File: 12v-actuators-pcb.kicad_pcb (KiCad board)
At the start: 2 copper layers, 0 parts

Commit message: First placement draft
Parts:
- added C1: 10uF, Capacitor_SMD:C_0805_2012Metric, F.Cu at (27.5, 27.8)
- added C10: 100nF, Capacitor_SMD:C_0603_1608Metric, F.Cu at (61.2, 10.8)
- added C11: 100nF, Capacitor_SMD:C_0603_1608Metric, F.Cu at (61.2, 13.3)
- added C12: 10uF, Capacitor_SMD:C_0805_2012Metric, F.Cu at (81.7, 11.2)
- added C13: 470pF, Capacitor_SMD:C_0603_1608Metric, F.Cu at (61.2, 15.8)
- added C14: 470pF, Capacitor_SMD:C_0603_1608Metric, F.Cu at (65.2, 0.76)
- added C15: 100nF, Capacitor_SMD:C_0603_1608Metric, F.Cu at (65.2, 3.27)
- added C16: 470pF, Capacitor_SMD:C_0603_1608Metric, F.Cu at (65.2, 5.78)
- added C17: 100nF, Capacitor_SMD:C_0603_1608Metric, F.Cu at (35.9, 53.3)
- added C18: 470uF, Capacitor_THT:C_Radial_D8.0mm_H11.5mm_P3.50mm, F.Cu at (187.5, 117.2)
- added C19: 470uF, Capacitor_THT:C_Radial_D8.0mm_H11.5mm_P3.50mm, F.Cu at (187.0, 107.8)
- added C2: 1nF, Capacitor_SMD:C_0603_1608Metric, F.Cu at (22.6, 43.7)
- added C20: 100nF, Capacitor_SMD:C_0603_1608Metric, F.Cu at (35.9, 55.8)
- added C21: 220nF, Capacitor_SMD:C_0603_1608Metric, F.Cu at (63.6, 62.9)
- added C22: 15nF, Capacitor_SMD:C_0603_1608Metric, F.Cu at (63.6, 65.5)
- added C23: 15nF, Capacitor_SMD:C_0603_1608Metric, F.Cu at (63.6, 68.0)
- added C24: 100nF, Capacitor_SMD:C_0603_1608Metric, F.Cu at (63.6, 70.5)
- added C25: 1uF, Capacitor_SMD:C_0805_2012Metric, F.Cu at (71.9, 70.4)
- added C3: 10uF, Capacitor_SMD:C_0805_2012Metric, F.Cu at (27.5, 30.8)
- added C4: 10uF, Capacitor_SMD:C_0805_2012Metric, F.Cu at (27.5, 33.8)
- added C5: 100nF, Capacitor_SMD:C_0603_1608Metric, F.Cu at (61.2, 0.76)
- added C6: 100nF, Capacitor_SMD:C_0603_1608Metric, F.Cu at (61.2, 3.27)
- added C7: 10uF, Capacitor_SMD:C_0805_2012Metric, F.Cu at (81.7, 8.21)
- added C8: 470pF, Capacitor_SMD:C_0603_1608Metric, F.Cu at (61.2, 5.78)
- added C9: 470pF, Capacitor_SMD:C_0603_1608Metric, F.Cu at (61.2, 8.29)
- added D1: ~, Diode_SMD:D_SOD-323, F.Cu at (77.4, 0.97)
- added D2: ~, Diode_SMD:D_SOD-323, F.Cu at (77.4, 3.92)
- added D3: ~, Diode_SMD:D_SOD-323, F.Cu at (77.4, 6.88)
- added D4: ~, Diode_SMD:D_SOD-323, F.Cu at (77.4, 9.82)
- added D5: ~, Diode_SMD:D_SOD-323, F.Cu at (77.4, 12.8)
- added D6: ~, ComponentsEvo:DO-214AB, F.Cu at (176.5, 106.5)
- added D7: 14.6V, Diode_SMD:D_SOD-323, F.Cu at (54.5, 72.2)
- added D8: LED, LED_SMD:LED_0603_1608Metric, F.Cu at (54.4, 75.0)
- added J1: 12V_C_MOT, ConnectorsEvo:691321100002, F.Cu at (196.0, 105.6)
- added J10: ESC_35_2_P, ConnectorsEvo:691321100002, F.Cu at (178.6, 66.3)
- added J11: MOTOR_15_2, Connector_PinHeader_2.54mm:PinHeader_1x03_P2.54mm_Vertical, F.Cu at (164.4, 74.0)
- added J12: ESC_35_2_S, Connector_PinHeader_2.54mm:PinHeader_1x03_P2.54mm_Vertical, F.Cu at (147.3, 63.8)
- added J13: MOTOR_15_3, Connector_PinHeader_2.54mm:PinHeader_1x03_P2.54mm_Vertical, F.Cu at (174.0, 74.0)
- added J14: 690367280876, ConnectorsEvo:690367280876, F.Cu at (156.8, 65.4)
- added J2: 3.5mm WR-TBL, ConnectorsEvo:691321100002, F.Cu at (196.0, 115.7)
- added J3: 690367280676, ConnectorsEvo:690367280676, F.Cu at (135.7, 65.5)
- added J4: LCD_DEG, Connector_PinHeader_2.54mm:PinHeader_1x03_P2.54mm_Vertical, F.Cu at (148.1, 74.0)
- added J5: CAN, Connector_PinHeader_2.54mm:PinHeader_1x02_P2.54mm_Vertical, F.Cu at (125.5, 69.2)
- added J6: ESC_35_1_P, ConnectorsEvo:691321100002, F.Cu at (168.8, 66.3)
- added J7: LED_EN, Connector_PinHeader_2.54mm:PinHeader_1x02_P2.54mm_Vertical, F.Cu at (134.0, 74.0)
- added J8: MOTOR_15_1, Connector_PinHeader_2.54mm:PinHeader_1x03_P2.54mm_Vertical, F.Cu at (154.3, 74.0)
- added J9: ESC_35_1_S, Connector_PinHeader_2.54mm:PinHeader_1x03_P2.54mm_Vertical, F.Cu at (143.5, 63.8)
- added Q1: G2302, Package_TO_SOT_SMD:SOT-23, F.Cu at (71.7, 29.0)
- added Q2: G2302, Package_TO_SOT_SMD:SOT-23, F.Cu at (71.7, 33.4)
- added Q3: G2302, Package_TO_SOT_SMD:SOT-23, F.Cu at (71.7, 37.9)
- added Q4: G2302, Package_TO_SOT_SMD:SOT-23, F.Cu at (71.7, 42.3)
- added Q5: G2302, Package_TO_SOT_SMD:SOT-23, F.Cu at (71.7, 46.8)
- added Q6: SUM110P06-08L, Package_TO_SOT_SMD:TO-252-2, F.Cu at (177.5, 115.2)
- added Q7: 2N7002, Package_TO_SOT_SMD:SOT-23, F.Cu at (49.9, 70.0)
- added Q8: 2N7002, Package_TO_SOT_SMD:SOT-23, F.Cu at (49.9, 74.5)
- added R1: 68, Resistor_SMD:R_0603_1608Metric, F.Cu at (22.6, 46.2)
- added R10: 22, Resistor_SMD:R_0603_1608Metric, F.Cu at (69.2, 8.29)
- added R11: 1k, Resistor_SMD:R_0603_1608Metric, F.Cu at (69.2, 10.8)
- added R12: 22, Resistor_SMD:R_0603_1608Metric, F.Cu at (69.2, 13.3)
- added R13: 10k, Resistor_SMD:R_0603_1608Metric, F.Cu at (69.2, 15.8)
- added R14: 1k, Resistor_SMD:R_0603_1608Metric, F.Cu at (73.2, 0.76)
- added R15: 10k, Resistor_SMD:R_0603_1608Metric, F.Cu at (73.2, 3.27)
- added R16: 1k, Resistor_SMD:R_0603_1608Metric, F.Cu at (73.2, 5.78)
- added R17: 10k, Resistor_SMD:R_0603_1608Metric, F.Cu at (73.2, 8.29)
- added R18: 10k, Resistor_SMD:R_0603_1608Metric, F.Cu at (35.9, 58.4)
- added R19: 0, Resistor_SMD:R_0603_1608Metric, F.Cu at (35.9, 60.9)
- added R2: 68, Resistor_SMD:R_0603_1608Metric, F.Cu at (22.6, 48.7)
- added R20: 4.7k, Resistor_SMD:R_0603_1608Metric, F.Cu at (35.9, 63.4)
- added R21: 10k, Resistor_SMD:R_0603_1608Metric, F.Cu at (35.9, 65.9)
- added R22: 10k, Resistor_SMD:R_0603_1608Metric, F.Cu at (35.9, 68.4)
- added R23: 10k, Resistor_SMD:R_0603_1608Metric, F.Cu at (35.9, 70.9)
- added R24: 0, Resistor_SMD:R_0805_2012Metric, F.Cu at (54.6, 69.3)
- added R25: 4.7k, Resistor_SMD:R_0603_1608Metric, F.Cu at (63.6, 73.0)
- added R26: 4.7k, Resistor_SMD:R_0603_1608Metric, F.Cu at (67.6, 62.9)
- added R27: 22, Resistor_SMD:R_0603_1608Metric, F.Cu at (67.6, 65.5)
- added R28: 100k, Resistor_SMD:R_0603_1608Metric, F.Cu at (67.6, 68.0)
- added R29: 100k, Resistor_SMD:R_0603_1608Metric, F.Cu at (67.6, 70.5)
- added R3: 22, Resistor_SMD:R_0603_1608Metric, F.Cu at (65.2, 8.29)
- added R30: 22, Resistor_SMD:R_0603_1608Metric, F.Cu at (67.6, 73.0)
- added R4: 1k, Resistor_SMD:R_0603_1608Metric, F.Cu at (65.2, 10.8)
- added R5: 10k, Resistor_SMD:R_0603_1608Metric, F.Cu at (65.2, 13.3)
- added R6: 22, Resistor_SMD:R_0603_1608Metric, F.Cu at (65.2, 15.8)
- added R7: 22, Resistor_SMD:R_0603_1608Metric, F.Cu at (69.2, 0.76)
- added R8: 1k, Resistor_SMD:R_0603_1608Metric, F.Cu at (69.2, 3.27)
- added R9: 10k, Resistor_SMD:R_0603_1608Metric, F.Cu at (69.2, 5.78)
- added TH1: NTC, Connector_PinHeader_2.54mm:PinHeader_1x02_P2.54mm_Vertical, F.Cu at (190.5, 72.4)
- added U1: MCP2551-I-SN, Package_SO:SOIC-8_3.9x4.9mm_P1.27mm, F.Cu at (131.5, 95.5)
- added U2: NUCLEO-F303K8, ComponentsEvo:MODULE_NUCLEO-F303K8, F.Cu at (133.8, 111.4)
- added U3: WSEN-PDUS, ComponentsEvo:WSEN-PDUS_2513130810X01, F.Cu at (96.0, 109.5)
- added X1: ESC_Emax_Bullet_15A, ComponentsEvo:ESC_Emax_Bullet_15A, F.Cu at (180.3, 88.4)
- added X2: ESC_Emax_Bullet_15A, ComponentsEvo:ESC_Emax_Bullet_15A, F.Cu at (147.8, 88.4)
- added X3: ESC_Emax_Bullet_15A, ComponentsEvo:ESC_Emax_Bullet_15A, F.Cu at (164.1, 88.4)
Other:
- board outline added: 120 x 60 mm

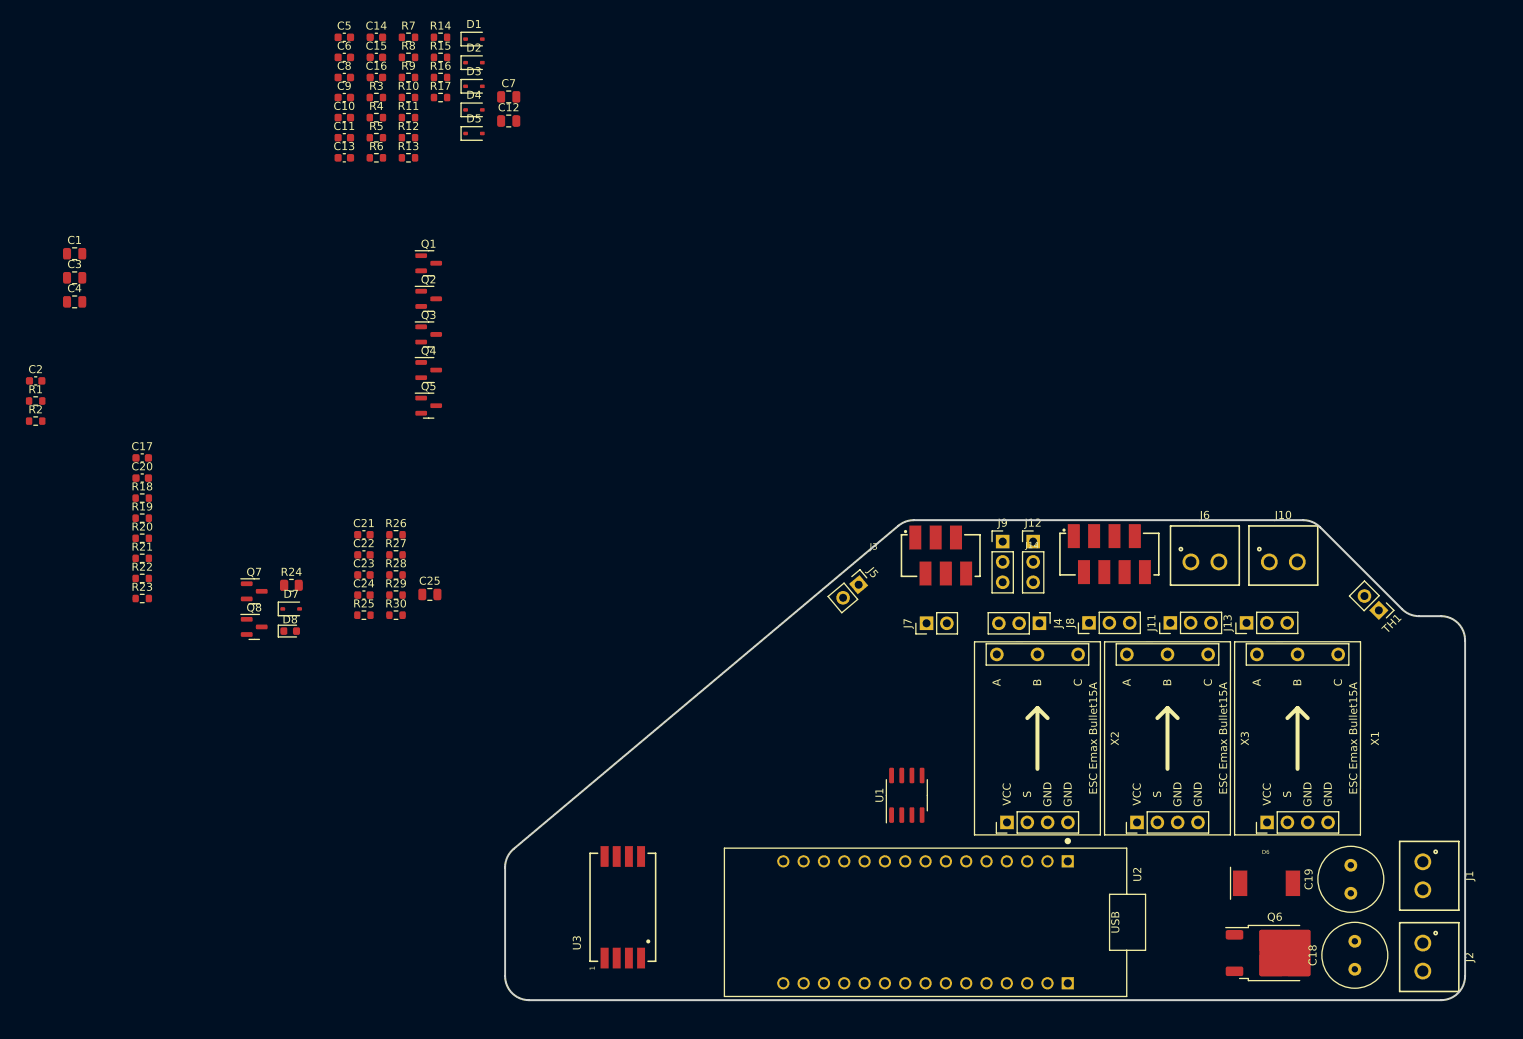
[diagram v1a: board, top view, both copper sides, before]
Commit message: Update schematic pinout for LED_EN + Add mechanical constraints to PCB layout
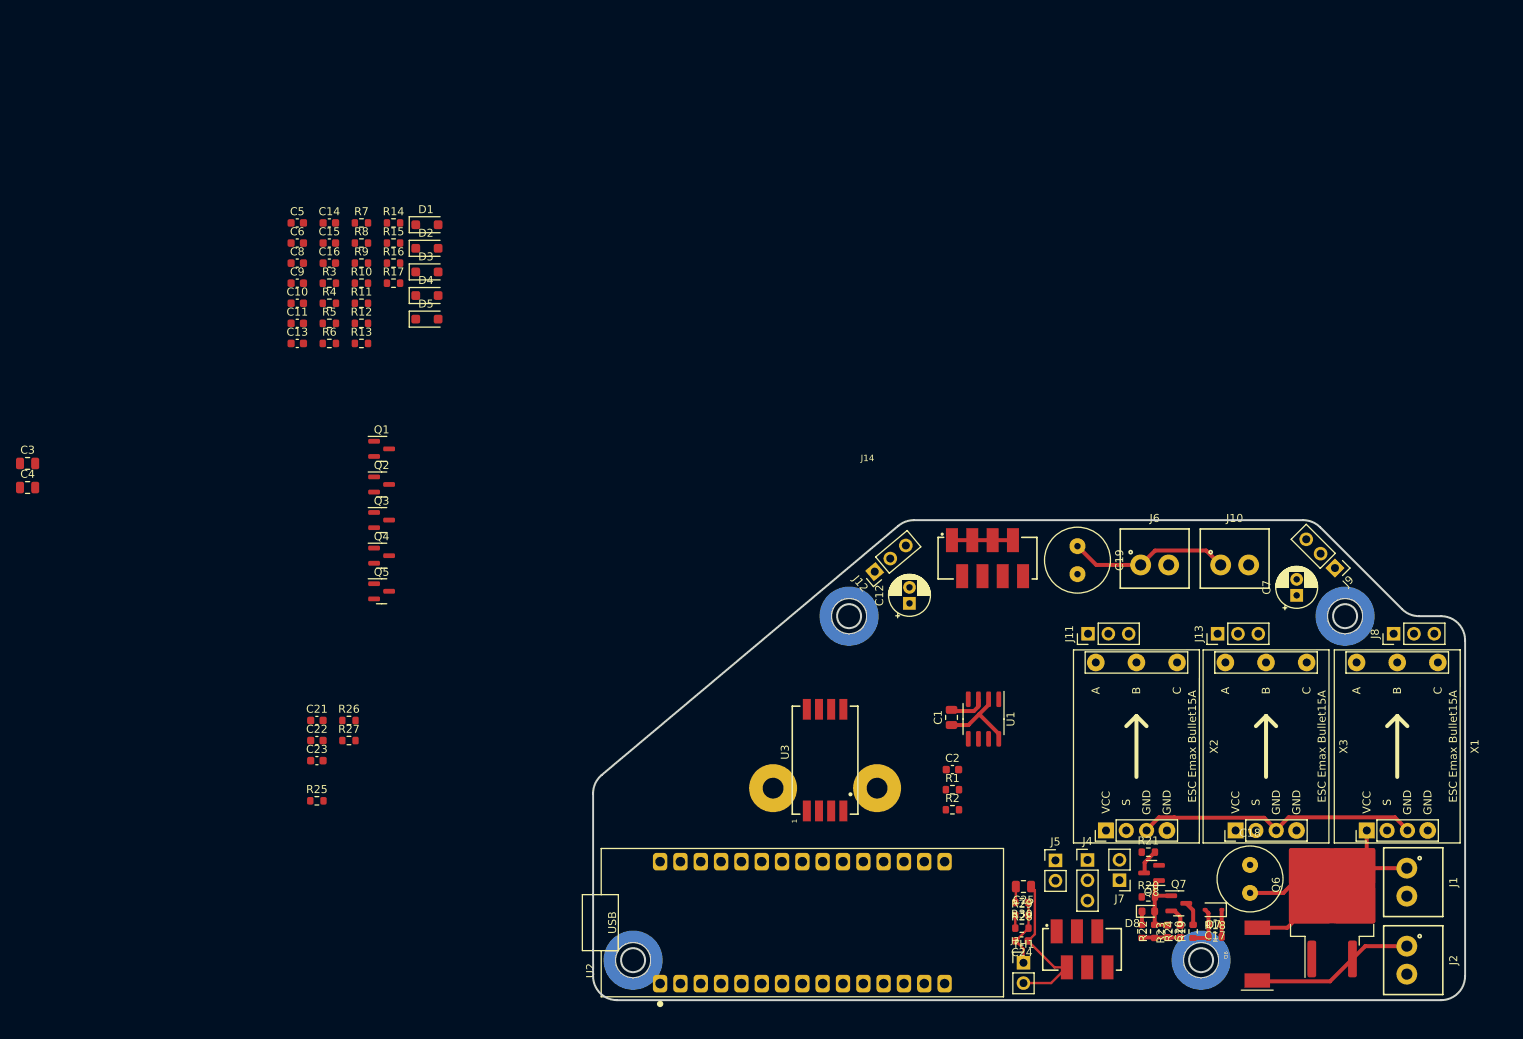
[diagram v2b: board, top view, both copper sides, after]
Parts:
- added REF**: Mounting_Wuerth_WA-SMSI-M3_H1.5mm_9774015360, Mounting_Wuerth:Mounting_Wuerth_WA-SMSI-M3_H1.5mm_9774015360, B.Cu at (124.3, 73.1)
- added REF**: Mounting_Wuerth_WA-SMSI-M3_H1.5mm_9774015360, Mounting_Wuerth:Mounting_Wuerth_WA-SMSI-M3_H1.5mm_9774015360, B.Cu at (168.3, 116.1)
- added REF**: Mounting_Wuerth_WA-SMSI-M3_H1.5mm_9774015360, Mounting_Wuerth:Mounting_Wuerth_WA-SMSI-M3_H1.5mm_9774015360, B.Cu at (186.3, 73.1)
- added REF**: Mounting_Wuerth_WA-SMSI-M3_H1.5mm_9774015360, Mounting_Wuerth:Mounting_Wuerth_WA-SMSI-M3_H1.5mm_9774015360, B.Cu at (97.3, 116.1)
- C12, C7: footprint Capacitor_SMD:C_0805_2012Metric -> Capacitor_THT:CP_Radial_D5.0mm_P2.00mm
- D1, D2, D3, D4, D5: footprint Diode_SMD:D_SOD-323 -> Diode_SMD:D_SOD-123F
- Q6: footprint Package_TO_SOT_SMD:TO-252-2 -> Package_TO_SOT_SMD:TO-263-2
- R24: footprint Resistor_SMD:R_0805_2012Metric -> Capacitor_SMD:C_0603_1608Metric
- moved C17 146.2 mm to (170.0, 111.6), turned to 180 degrees
- moved R18 144.9 mm to (170.0, 113.2)
- moved R19 141.1 mm to (167.3, 112.5), turned to 90 degrees
- moved C20 140.1 mm to (164.1, 112.5), turned to -90 degrees
- moved R22 134.0 mm to (162.5, 112.5), turned to 90 degrees
- moved R20 133.5 mm to (161.7, 108.2)
- moved R23 131.7 mm to (160.9, 112.5), turned to -90 degrees
- moved R21 131.0 mm to (161.7, 102.6)
- moved C2 124.5 mm to (137.2, 92.3)
- moved R2 124.5 mm to (137.2, 97.3)
- moved R1 124.5 mm to (137.2, 94.8)
- moved C1 124.0 mm to (137.1, 85.8), turned to 90 degrees
- moved Q7 122.0 mm to (165.5, 109.0)
- moved D7 121.3 mm to (169.8, 109.8), turned to 180 degrees
- moved R24 119.2 mm to (165.7, 112.5), turned to 90 degrees
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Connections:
- U2 pad 1.15: unconnected-(U2-PB4-Pad1.15) -> /LED_EN
- U2 pad 2.5: /LED_EN -> unconnected-(U2-PA2-Pad2.5)
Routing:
- net GND: track 0.00 -> 70.3 mm
- net /PWR_12V: track 0.00 -> 56.5 mm
- net /VBATT_12V: track 0.00 -> 24.0 mm
- net /Arrêt d'urgence/SW_AU/2: track 0.00 -> 9.47 mm
- net Net-(C24-Pad2): track 0.00 -> 8.59 mm
- net Net-(D7-A): track 0.00 -> 5.21 mm
- net +5V: track 0.00 -> 4.57 mm
- net /AU_STATUS: track 0.00 -> 3.21 mm
- net Net-(Q7-D): track 0.00 -> 3.04 mm
- net GNDPWR: track 0.00 -> 2.50 mm
- net /A_TEMP: track 0.00 -> 2.03 mm
- net Net-(D8-K): track 0.00 -> 1.68 mm
- net +3.3V: track 0.00 -> 1.60 mm
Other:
- board size 120 x 60 mm -> 109 x 60 mm

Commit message: New PCB reorganisation around mechanical constraints
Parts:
- moved C3 51.7 mm to (68.6, 75.6)
- moved C4 51.7 mm to (68.6, 78.6)
- moved R14 23.2 mm to (86.3, 37.4)
- moved R15 23.2 mm to (86.3, 39.9)
- moved R16 23.2 mm to (86.3, 42.4)
- moved R17 23.2 mm to (86.3, 44.9)
- moved C10 23.2 mm to (74.2, 47.4)
- moved C11 23.2 mm to (74.2, 49.9)
- moved C5 23.2 mm to (74.2, 37.4)
- moved C6 23.2 mm to (74.2, 39.9)
- moved C8 23.2 mm to (74.2, 42.4)
- moved C9 23.2 mm to (74.2, 44.9)
- moved C13 23.2 mm to (74.2, 52.4)
- moved C14 23.2 mm to (78.3, 37.4)
- moved C15 23.2 mm to (78.3, 39.9)
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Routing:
- net /PWR_12V: track 56.5 -> 32.4 mm
- net Net-(D7-A): track 5.21 -> 18.6 mm
- net Net-(D1-A): track 0.00 -> 11.0 mm
- net /VBATT_12V: track 24.0 -> 32.2 mm
- net /SW_AU: track 0.00 -> 6.12 mm
- net Net-(C24-Pad2): track 8.59 -> 5.46 mm
- net GNDPWR: track 2.50 -> 0.00 mm
- net GND: track 70.3 -> 68.4 mm
- net Net-(Q7-D): track 3.04 -> 3.69 mm
- net Net-(D8-K): track 1.68 -> 2.23 mm
